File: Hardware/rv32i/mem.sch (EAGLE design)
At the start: 8 parts, among them IC1 IS61C5128AS-25QLI, IC2 IS61C5128AS-25QLI, IC3 IS61C5128AS-25QLI, IC4 IS61C5128AS-25QLI, IC5 IS61C5128AS-25QLI, IC6 IS61C5128AS-25QLI, IC7 IS61C5128AS-25QLI, IC8 IS61C5128AS-25QLI

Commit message: Ram schematic
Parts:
- added C1, C2, C3, C4, C5, C6, C7, C8, C9: CC0603KRX7R9BB104, CC0603KRX7R9BB104:CC0603KRX7R9BB104
- added IC10, IC9: SN74HC138PWR, SN74HC138PWR:SN74HC138PWR
- added JP1, JP2, JP3, JP4, JP5, JP6: (no value), pinhead:PINHD-2X20
- added R1, R2: RC0603FR-0710KL, RC0603FR-0710KL:RC0603FR-0710KL
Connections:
- removed net A0: IC1.A0, IC2.A0, IC3.A0, IC4.A0, IC5.A0, IC6.A0, IC7.A0, IC8.A0
- removed net A1: IC1.A1, IC2.A1, IC3.A1, IC4.A1, IC5.A1, IC6.A1, IC7.A1, IC8.A1
- removed net A10: IC1.A10, IC2.A10, IC3.A10, IC4.A10, IC5.A10, IC6.A10, IC7.A10, IC8.A10
- removed net A11: IC1.A11, IC2.A11, IC3.A11, IC4.A11, IC5.A11, IC6.A11, IC7.A11, IC8.A11
- removed net A12: IC1.A12, IC2.A12, IC3.A12, IC4.A12, IC5.A12, IC6.A12, IC7.A12, IC8.A12
- removed net A13: IC1.A13, IC2.A13, IC3.A13, IC4.A13, IC5.A13, IC6.A13, IC7.A13, IC8.A13
- removed net A14: IC1.A14, IC2.A14, IC3.A14, IC4.A14, IC5.A14, IC6.A14, IC7.A14, IC8.A14
- removed net A15: IC1.A15, IC2.A15, IC3.A15, IC4.A15, IC5.A15, IC6.A15, IC7.A15, IC8.A15
- removed net A16: IC1.A16, IC2.A16, IC3.A16, IC4.A16, IC5.A16, IC6.A16, IC7.A16, IC8.A16
- removed net A17: IC1.A17, IC2.A17, IC3.A17, IC4.A17, IC5.A17, IC6.A17, IC7.A17, IC8.A17
- removed net A18: IC1.A18, IC2.A18, IC3.A18, IC4.A18, IC5.A18, IC6.A18, IC7.A18, IC8.A18
- removed net A2: IC1.A2, IC2.A2, IC3.A2, IC4.A2, IC5.A2, IC6.A2, IC7.A2, IC8.A2
- removed net A3: IC1.A3, IC2.A3, IC3.A3, IC4.A3, IC5.A3, IC6.A3, IC7.A3, IC8.A3
- removed net A4: IC1.A4, IC2.A4, IC3.A4, IC4.A4, IC5.A4, IC6.A4, IC7.A4, IC8.A4
- removed net A5: IC1.A5, IC2.A5, IC3.A5, IC4.A5, IC5.A5, IC6.A5, IC7.A5, IC8.A5
- removed net A6: IC1.A6, IC2.A6, IC3.A6, IC4.A6, IC5.A6, IC6.A6, IC7.A6, IC8.A6
- removed net A7: IC1.A7, IC2.A7, IC3.A7, IC4.A7, IC5.A7, IC6.A7, IC7.A7, IC8.A7
- removed net A8: IC1.A8, IC2.A8, IC3.A8, IC4.A8, IC5.A8, IC6.A8, IC7.A8, IC8.A8
- removed net A9: IC1.A9, IC2.A9, IC3.A9, IC4.A9, IC5.A9, IC6.A9, IC7.A9, IC8.A9
- removed net D0: IC1.I/O0, IC2.I/O0, IC3.I/O0, IC4.I/O0, IC5.I/O0, IC6.I/O0, IC7.I/O0, IC8.I/O0
- removed net D1: IC1.I/O1, IC2.I/O1, IC3.I/O1, IC4.I/O1, IC5.I/O1, IC6.I/O1, IC7.I/O1, IC8.I/O1
- removed net D2: IC1.I/O2, IC2.I/O2, IC3.I/O2, IC4.I/O2, IC5.I/O2, IC6.I/O2, IC7.I/O2, IC8.I/O2
- removed net D3: IC1.I/O3, IC2.I/O3, IC3.I/O3, IC4.I/O3, IC5.I/O3, IC6.I/O3, IC7.I/O3, IC8.I/O3
- removed net D4: IC1.I/O4, IC2.I/O4, IC3.I/O4, IC4.I/O4, IC5.I/O4, IC6.I/O4, IC7.I/O4, IC8.I/O4
- removed net D5: IC1.I/O5, IC2.I/O5, IC3.I/O5, IC4.I/O5, IC5.I/O5, IC6.I/O5, IC7.I/O5, IC8.I/O5
- removed net D6: IC1.I/O6, IC2.I/O6, IC3.I/O6, IC4.I/O6, IC5.I/O6, IC6.I/O6, IC7.I/O6, IC8.I/O6
- removed net D7: IC1.I/O7, IC2.I/O7, IC3.I/O7, IC4.I/O7, IC5.I/O7, IC6.I/O7, IC7.I/O7, IC8.I/O7
- new net B0_A0: IC2.A0, IC6.A0, IC7.A0, IC8.A0, JP1.5, JP2.5
- new net B0_A1: IC2.A1, IC6.A1, IC7.A1, IC8.A1, JP1.7, JP2.7
- new net B0_A10: IC2.A10, IC6.A10, IC7.A10, IC8.A10, JP1.25, JP2.25
- new net B0_A11: IC2.A11, IC6.A11, IC7.A11, IC8.A11, JP1.27, JP2.27
- new net B0_A12: IC2.A12, IC6.A12, IC7.A12, IC8.A12, JP1.29, JP2.29
- new net B0_A13: IC2.A13, IC6.A13, IC7.A13, IC8.A13, JP1.31, JP2.31
- new net B0_A14: IC2.A14, IC6.A14, IC7.A14, IC8.A14, JP1.33, JP2.33
- new net B0_A15: IC2.A15, IC6.A15, IC7.A15, IC8.A15, JP1.35, JP2.35
- new net B0_A16: IC2.A16, IC6.A16, IC7.A16, IC8.A16, JP1.6, JP2.6
- new net B0_A17: IC2.A17, IC6.A17, IC7.A17, IC8.A17, JP1.8, JP2.8
- new net B0_A18: IC2.A18, IC6.A18, IC7.A18, IC8.A18, JP1.10, JP2.10
- new net B0_A19: IC9.A, JP1.12, JP2.12
- new net B0_A2: IC2.A2, IC6.A2, IC7.A2, IC8.A2, JP1.9, JP2.9
- new net B0_A20: IC9.B, JP1.14, JP2.14
- new net B0_A21: JP1.16, JP2.16
- new net B0_A22: JP1.18, JP2.18
- new net B0_A23: JP1.20, JP2.20
- new net B0_A24: JP1.22, JP2.22
- new net B0_A25: JP1.24, JP2.24
- new net B0_A26: JP1.26, JP2.26
- new net B0_A27: JP1.28, JP2.28
- new net B0_A28: JP1.30, JP2.30
- new net B0_A29: JP1.32, JP2.32
- new net B0_A3: IC2.A3, IC6.A3, IC7.A3, IC8.A3, JP1.11, JP2.11
- new net B0_A30: JP1.34, JP2.34
- new net B0_A31: JP1.36, JP2.36
- new net B0_A4: IC2.A4, IC6.A4, IC7.A4, IC8.A4, JP1.13, JP2.13
- new net B0_A5: IC2.A5, IC6.A5, IC7.A5, IC8.A5, JP1.15, JP2.15
- new net B0_A6: IC2.A6, IC6.A6, IC7.A6, IC8.A6, JP1.17, JP2.17
- new net B0_A7: IC2.A7, IC6.A7, IC7.A7, IC8.A7, JP1.19, JP2.19
- new net B0_A8: IC2.A8, IC6.A8, IC7.A8, IC8.A8, JP1.21, JP2.21
- new net B0_A9: IC2.A9, IC6.A9, IC7.A9, IC8.A9, JP1.23, JP2.23
- new net B0_D0: IC2.I/O0, IC6.I/O0, IC7.I/O0, IC8.I/O0, JP4.5, JP6.5
- new net B0_D1: IC2.I/O1, IC6.I/O1, IC7.I/O1, IC8.I/O1, JP4.7, JP6.7
- new net B0_D2: IC2.I/O2, IC6.I/O2, IC7.I/O2, IC8.I/O2, JP4.9, JP6.9
- new net B0_D3: IC2.I/O3, IC6.I/O3, IC7.I/O3, IC8.I/O3, JP4.11, JP6.11
- new net B0_D4: IC2.I/O4, IC6.I/O4, IC7.I/O4, IC8.I/O4, JP4.13, JP6.13
- new net B0_D5: IC2.I/O5, IC6.I/O5, IC7.I/O5, IC8.I/O5, JP4.15, JP6.15
- new net B0_D6: IC2.I/O6, IC6.I/O6, IC7.I/O6, IC8.I/O6, JP4.17, JP6.17
- new net B0_D7: IC2.I/O7, IC6.I/O7, IC7.I/O7, IC8.I/O7, JP4.19, JP6.19
- new net B1_A0: IC1.A0, IC3.A0, IC4.A0, IC5.A0, JP3.5, JP5.5
- new net B1_A1: IC1.A1, IC3.A1, IC4.A1, IC5.A1, JP3.7, JP5.7
- new net B1_A10: IC1.A10, IC3.A10, IC4.A10, IC5.A10, JP3.25, JP5.25
- new net B1_A11: IC1.A11, IC3.A11, IC4.A11, IC5.A11, JP3.27, JP5.27
- new net B1_A12: IC1.A12, IC3.A12, IC4.A12, IC5.A12, JP3.29, JP5.29
- new net B1_A13: IC1.A13, IC3.A13, IC4.A13, IC5.A13, JP3.31, JP5.31
- new net B1_A14: IC1.A14, IC3.A14, IC4.A14, IC5.A14, JP3.33, JP5.33
- new net B1_A15: IC1.A15, IC3.A15, IC4.A15, IC5.A15, JP3.35, JP5.35
- new net B1_A16: IC1.A16, IC3.A16, IC4.A16, IC5.A16, JP3.6, JP5.6
- new net B1_A17: IC1.A17, IC3.A17, IC4.A17, IC5.A17, JP3.8, JP5.8
- new net B1_A18: IC1.A18, IC3.A18, IC4.A18, IC5.A18, JP3.10, JP5.10
- new net B1_A19: IC10.A, JP3.12, JP5.12
- new net B1_A2: IC1.A2, IC3.A2, IC4.A2, IC5.A2, JP3.9, JP5.9
- new net B1_A20: IC10.B, JP3.14, JP5.14
- new net B1_A21: JP3.16, JP5.16
- new net B1_A22: JP3.18, JP5.18
- new net B1_A23: JP3.20, JP5.20
- new net B1_A24: JP3.22, JP5.22
- new net B1_A25: JP3.24, JP5.24
- new net B1_A26: JP3.26, JP5.26
- new net B1_A27: JP3.28, JP5.28
- new net B1_A28: JP3.30, JP5.30
- new net B1_A29: JP3.32, JP5.32
- new net B1_A3: IC1.A3, IC3.A3, IC4.A3, IC5.A3, JP3.11, JP5.11
- new net B1_A30: JP3.34, JP5.34
- new net B1_A31: JP3.36, JP5.36
- new net B1_A4: IC1.A4, IC3.A4, IC4.A4, IC5.A4, JP3.13, JP5.13
- new net B1_A5: IC1.A5, IC3.A5, IC4.A5, IC5.A5, JP3.15, JP5.15
- new net B1_A6: IC1.A6, IC3.A6, IC4.A6, IC5.A6, JP3.17, JP5.17
- new net B1_A7: IC1.A7, IC3.A7, IC4.A7, IC5.A7, JP3.19, JP5.19
- new net B1_A8: IC1.A8, IC3.A8, IC4.A8, IC5.A8, JP3.21, JP5.21
- new net B1_A9: IC1.A9, IC3.A9, IC4.A9, IC5.A9, JP3.23, JP5.23
- new net B1_D0: IC1.I/O0, IC3.I/O0, IC4.I/O0, IC5.I/O0, JP4.6, JP6.6
- new net B1_D1: IC1.I/O1, IC3.I/O1, IC4.I/O1, IC5.I/O1, JP4.8, JP6.8
- new net B1_D2: IC1.I/O2, IC3.I/O2, IC4.I/O2, IC5.I/O2, JP4.10, JP6.10
- new net B1_D3: IC1.I/O3, IC3.I/O3, IC4.I/O3, IC5.I/O3, JP4.12, JP6.12
- new net B1_D4: IC1.I/O4, IC3.I/O4, IC4.I/O4, IC5.I/O4, JP4.14, JP6.14
- new net B1_D5: IC1.I/O5, IC3.I/O5, IC4.I/O5, IC5.I/O5, JP4.16, JP6.16
- new net B1_D6: IC1.I/O6, IC3.I/O6, IC4.I/O6, IC5.I/O6, JP4.18, JP6.18
- new net B1_D7: IC1.I/O7, IC3.I/O7, IC4.I/O7, IC5.I/O7, JP4.20, JP6.20
- new net CE4: IC10.Y0, IC5.!CE
- new net CE5: IC1.!CE, IC10.Y1
- new net CE6: IC10.Y2, IC3.!CE
- new net CE7: IC10.Y3, IC4.!CE
- net CE0: now also IC9.Y0; no longer IC5.!CE
- net CE1: now also IC9.Y1; no longer IC1.!CE
- net CE2: now also IC9.Y2; no longer IC3.!CE
- net CE3: now also IC9.Y3; no longer IC4.!CE
- net GND: now also C1.1, C2.1, C3.1, C4.1, C5.1, C6.1, C7.1, C8.1, C9.1, IC10.!G2A, IC10.!G2B, IC10.C, IC10.GND, IC9.!G2A, IC9.!G2B, IC9.C, IC9.GND, JP1.3, JP1.37, JP1.38, JP1.4, JP2.3, JP2.37, JP2.38, JP2.4, JP3.3, JP3.37, JP3.38, JP3.4, JP4.3, JP4.37, JP4.38, JP4.4, JP5.3, JP5.37, JP5.38, JP5.4, JP6.3, JP6.37, JP6.38, JP6.4, R1.2, R2.2
- net VCC: now also C1.2, C2.2, C3.2, C4.2, C5.2, C6.2, C7.2, C8.2, C9.2, IC10.G1, IC10.VCC, IC9.G1, IC9.VCC, JP1.1, JP1.2, JP1.39, JP1.40, JP2.1, JP2.2, JP2.39, JP2.40, JP3.1, JP3.2, JP3.39, JP3.40, JP4.1, JP4.2, JP4.39, JP4.40, JP5.1, JP5.2, JP5.39, JP5.40, JP6.1, JP6.2, JP6.39, JP6.40
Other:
- note added: "Chip selector"
- note added: "Headers"
- note added: "Passive Components"

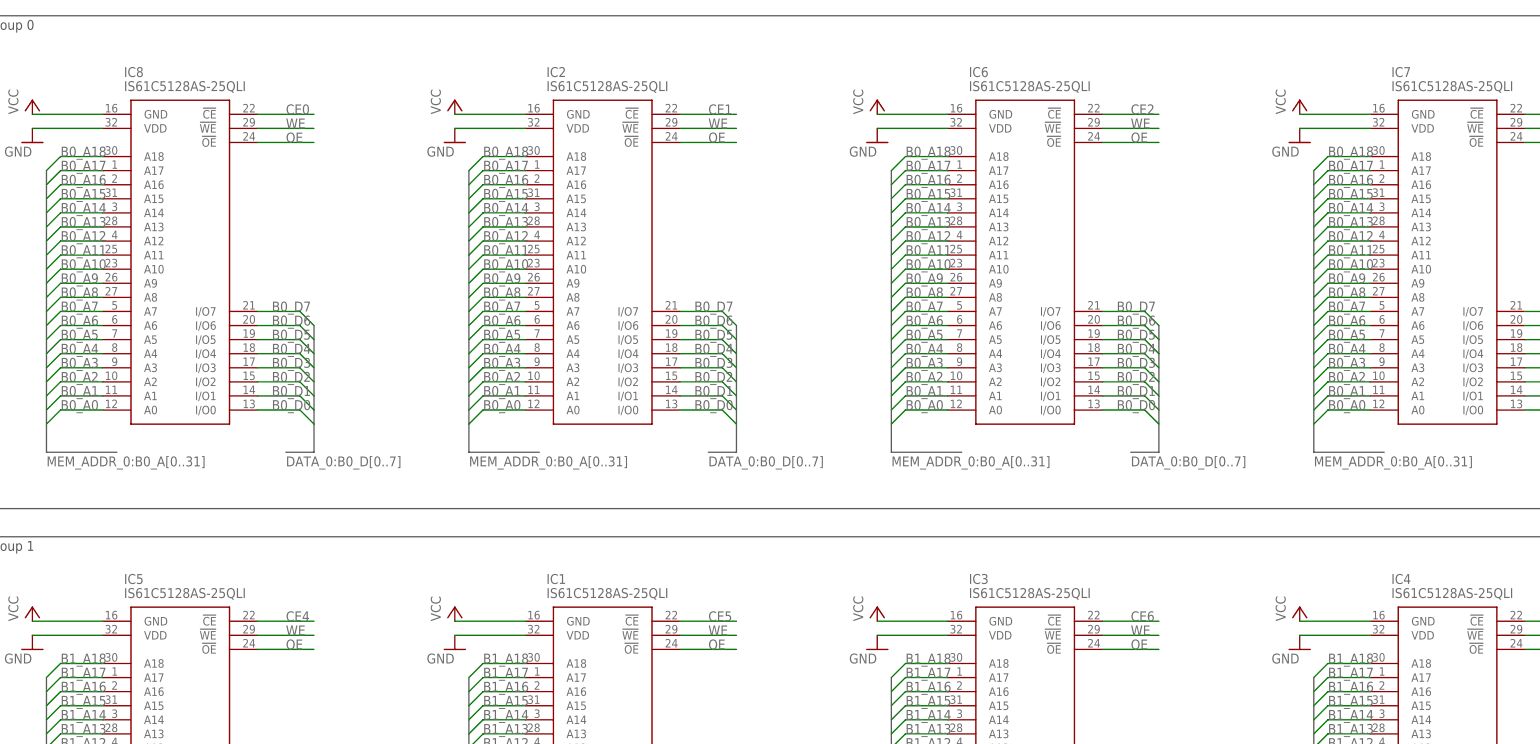
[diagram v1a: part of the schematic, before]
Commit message: Memory pcb layout
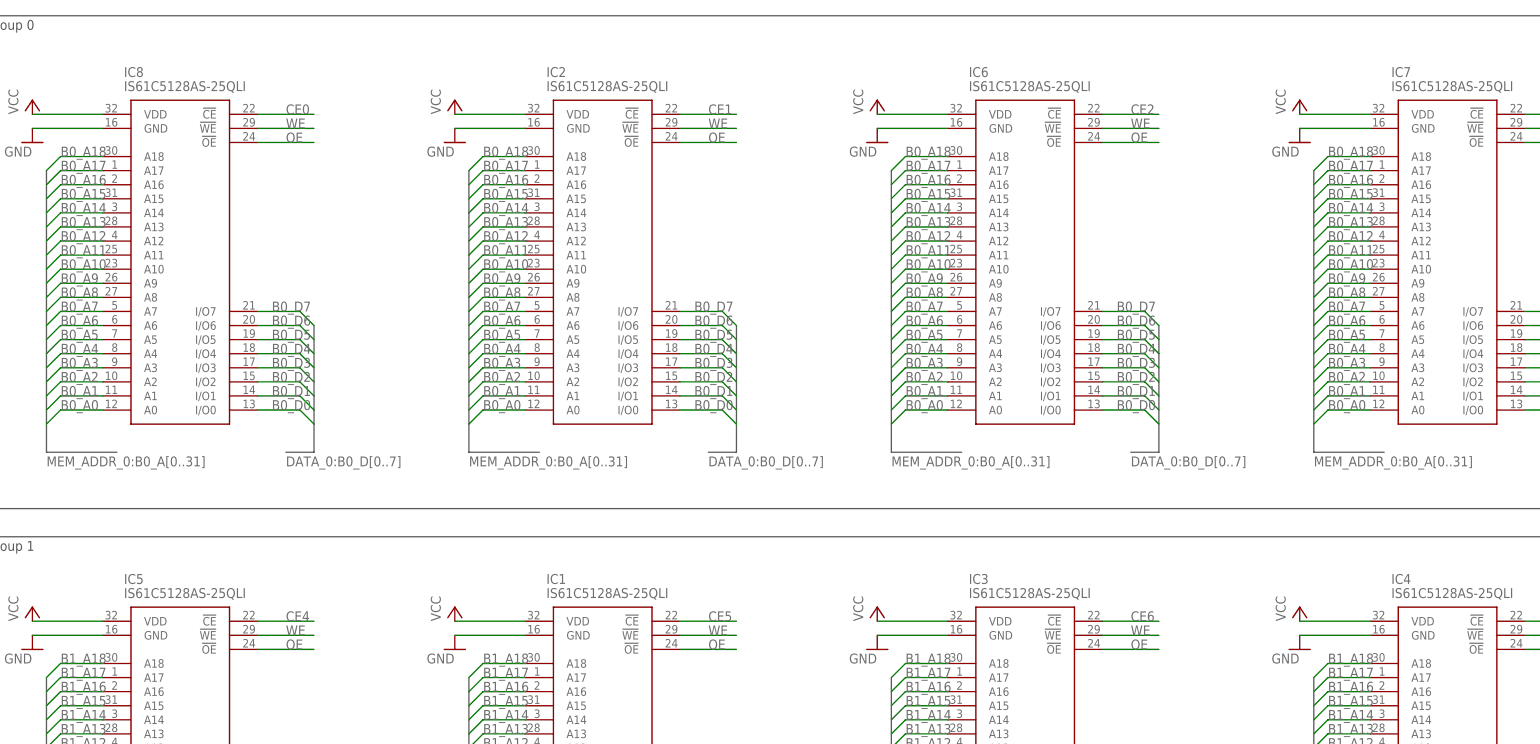
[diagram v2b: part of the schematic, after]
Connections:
- net GND: now also IC1.GND, IC2.GND, IC3.GND, IC4.GND, IC5.GND, IC6.GND, IC7.GND, IC8.GND; no longer IC1.VDD, IC2.VDD, IC3.VDD, IC4.VDD, IC5.VDD, IC6.VDD, IC7.VDD, IC8.VDD
- net VCC: now also IC1.VDD, IC2.VDD, IC3.VDD, IC4.VDD, IC5.VDD, IC6.VDD, IC7.VDD, IC8.VDD; no longer IC1.GND, IC2.GND, IC3.GND, IC4.GND, IC5.GND, IC6.GND, IC7.GND, IC8.GND
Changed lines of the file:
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@@
 <net name="VCC" class="0">
 <segment>
-<pinref part="IC5" gate="G$1" pin="GND"/>
+<pinref part="IC5" gate="G$1" pin="VDD"/>
 <pinref part="P+4" gate="VCC" pin="VCC"/>
 <wire x1="30.48" y1="73.66" x2="17.78" y2="73.66" width="0.1524" layer="91"/>
 </segment>
 <segment>
-<pinref part="IC2" gate="G$1" pin="GND"/>
+<pinref part="IC2" gate="G$1" pin="VDD"/>
 <pinref part="P+5" gate="VCC" pin="VCC"/>
 <wire x1="106.68" y1="165.1" x2="93.98" y2="165.1" width="0.1524" layer="91"/>
 </segment>
 <segment>
-<pinref part="IC6" gate="G$1" pin="GND"/>
+<pinref part="IC6" gate="G$1" pin="VDD"/>
 <pinref part="P+6" gate="VCC" pin="VCC"/>
 <wire x1="182.88" y1="165.1" x2="170.18" y2="165.1" width="0.1524" layer="91"/>
 </segment>
 <segment>
-<pinref part="IC7" gate="G$1" pin="GND"/>
+<pinref part="IC7" gate="G$1" pin="VDD"/>
 <pinref part="P+7" gate="VCC" pin="VCC"/>
 <wire x1="259.08" y1="165.1" x2="246.38" y2="165.1" width="0.1524" layer="91"/>
 </segment>
 <segment>
-<pinref part="IC8" gate="G$1" pin="GND"/>
+<pinref part="IC8" gate="G$1" pin="VDD"/>
 <pinref part="P+8" gate="VCC" pin="VCC"/>
 <wire x1="30.48" y1="165.1" x2="17.78" y2="165.1" width="0.1524" layer="91"/>
@@
 </segment>
 <segment>
-<pinref part="IC1" gate="G$1" pin="GND"/>
+<pinref part="IC1" gate="G$1" pin="VDD"/>
 <pinref part="P+1" gate="VCC" pin="VCC"/>
 <wire x1="106.68" y1="73.66" x2="93.98" y2="73.66" width="0.1524" layer="91"/>
 </segment>
 <segment>
-<pinref part="IC3" gate="G$1" pin="GND"/>
+<pinref part="IC3" gate="G$1" pin="VDD"/>
 <pinref part="P+2" gate="VCC" pin="VCC"/>
 <wire x1="182.88" y1="73.66" x2="170.18" y2="73.66" width="0.1524" layer="91"/>
 </segment>
 <segment>
-<pinref part="IC4" gate="G$1" pin="GND"/>
+<pinref part="IC4" gate="G$1" pin="VDD"/>
 <pinref part="P+3" gate="VCC" pin="VCC"/>
 <wire x1="259.08" y1="73.66" x2="246.38" y2="73.66" width="0.1524" layer="91"/>
@@
 <net name="GND" class="0">
 <segment>
-<pinref part="IC5" gate="G$1" pin="VDD"/>
+<pinref part="IC5" gate="G$1" pin="GND"/>
 <pinref part="GND4" gate="1" pin="GND"/>
 <wire x1="30.48" y1="71.12" x2="17.78" y2="71.12" width="0.1524" layer="91"/>
 </segment>
 <segment>
-<pinref part="IC2" gate="G$1" pin="VDD"/>
+<pinref part="IC2" gate="G$1" pin="GND"/>
 <pinref part="GND5" gate="1" pin="GND"/>
 <wire x1="106.68" y1="162.56" x2="93.98" y2="162.56" width="0.1524" layer="91"/>
 </segment>
 <segment>
-<pinref part="IC6" gate="G$1" pin="VDD"/>
+<pinref part="IC6" gate="G$1" pin="GND"/>
 <pinref part="GND6" gate="1" pin="GND"/>
 <wire x1="182.88" y1="162.56" x2="170.18" y2="162.56" width="0.1524" layer="91"/>
 </segment>
 <segment>
-<pinref part="IC7" gate="G$1" pin="VDD"/>
+<pinref part="IC7" gate="G$1" pin="GND"/>
 <pinref part="GND7" gate="1" pin="GND"/>
 <wire x1="259.08" y1="162.56" x2="246.38" y2="162.56" width="0.1524" layer="91"/>
 </segment>
 <segment>
-<pinref part="IC8" gate="G$1" pin="VDD"/>
+<pinref part="IC8" gate="G$1" pin="GND"/>
 <pinref part="GND8" gate="1" pin="GND"/>
 <wire x1="30.48" y1="162.56" x2="17.78" y2="162.56" width="0.1524" layer="91"/>
@@
 </segment>
 <segment>
-<pinref part="IC1" gate="G$1" pin="VDD"/>
+<pinref part="IC1" gate="G$1" pin="GND"/>
 <pinref part="GND1" gate="1" pin="GND"/>
 <wire x1="106.68" y1="71.12" x2="93.98" y2="71.12" width="0.1524" layer="91"/>
 </segment>
 <segment>
-<pinref part="IC3" gate="G$1" pin="VDD"/>
+<pinref part="IC3" gate="G$1" pin="GND"/>
 <pinref part="GND2" gate="1" pin="GND"/>
 <wire x1="182.88" y1="71.12" x2="170.18" y2="71.12" width="0.1524" layer="91"/>
 </segment>
 <segment>
-<pinref part="IC4" gate="G$1" pin="VDD"/>
+<pinref part="IC4" gate="G$1" pin="GND"/>
 <pinref part="GND3" gate="1" pin="GND"/>
 <wire x1="259.08" y1="71.12" x2="246.38" y2="71.12" width="0.1524" layer="91"/>
